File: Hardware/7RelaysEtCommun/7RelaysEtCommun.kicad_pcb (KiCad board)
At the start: 2 copper layers, 67 x 93 mm, 41 parts, among them J1 5VIN, J10 ISP, J2 Conn_01x02_Female, J3 Conn_01x02_Female, J4 Conn_01x02_Female, J5 Conn_01x02_Female, J6 Conn_01x02_Female, J7 Conn_01x02_Female, J8 Conn_01x02_Female, K1 UMS05-1A80-75L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

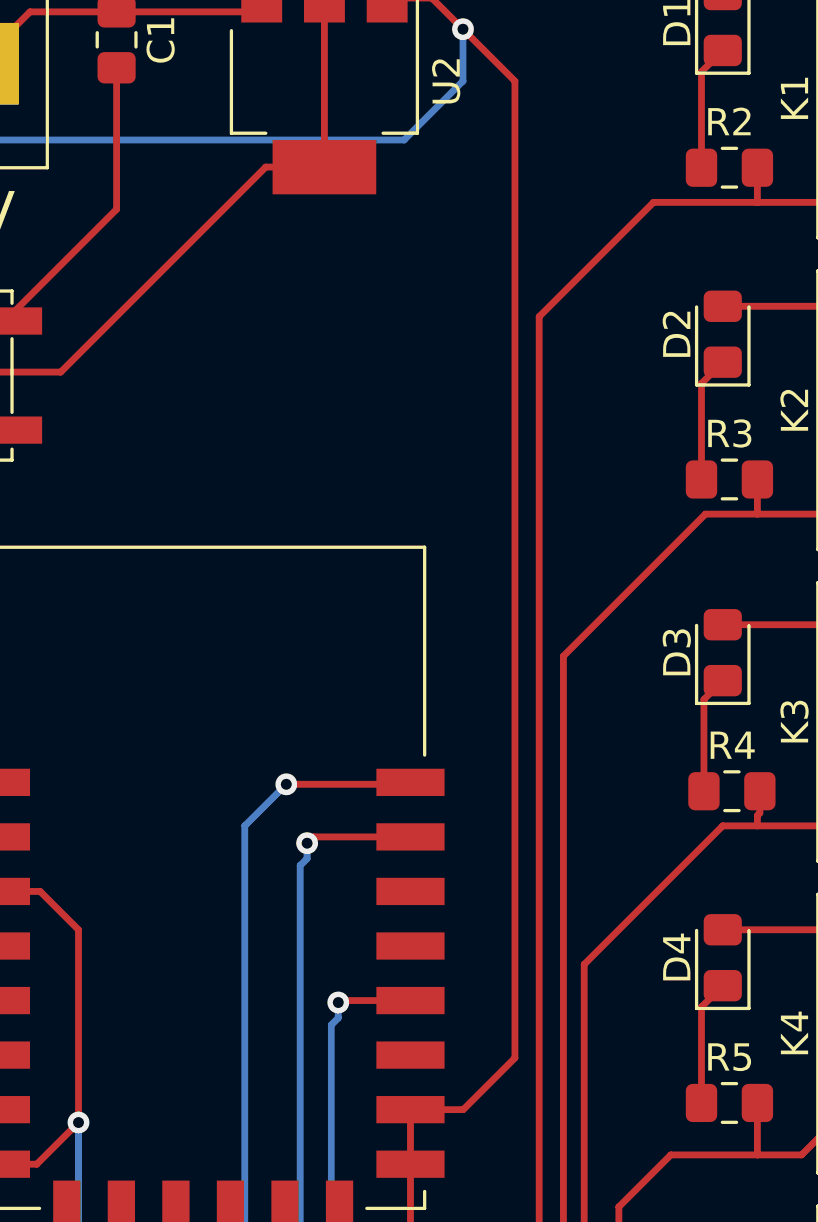
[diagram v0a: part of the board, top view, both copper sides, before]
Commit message: - Modified almost all hardware boards : They were missing a pull-up resistor on GPIO2, which made impossible to flash. - Updated baseBoard.* files
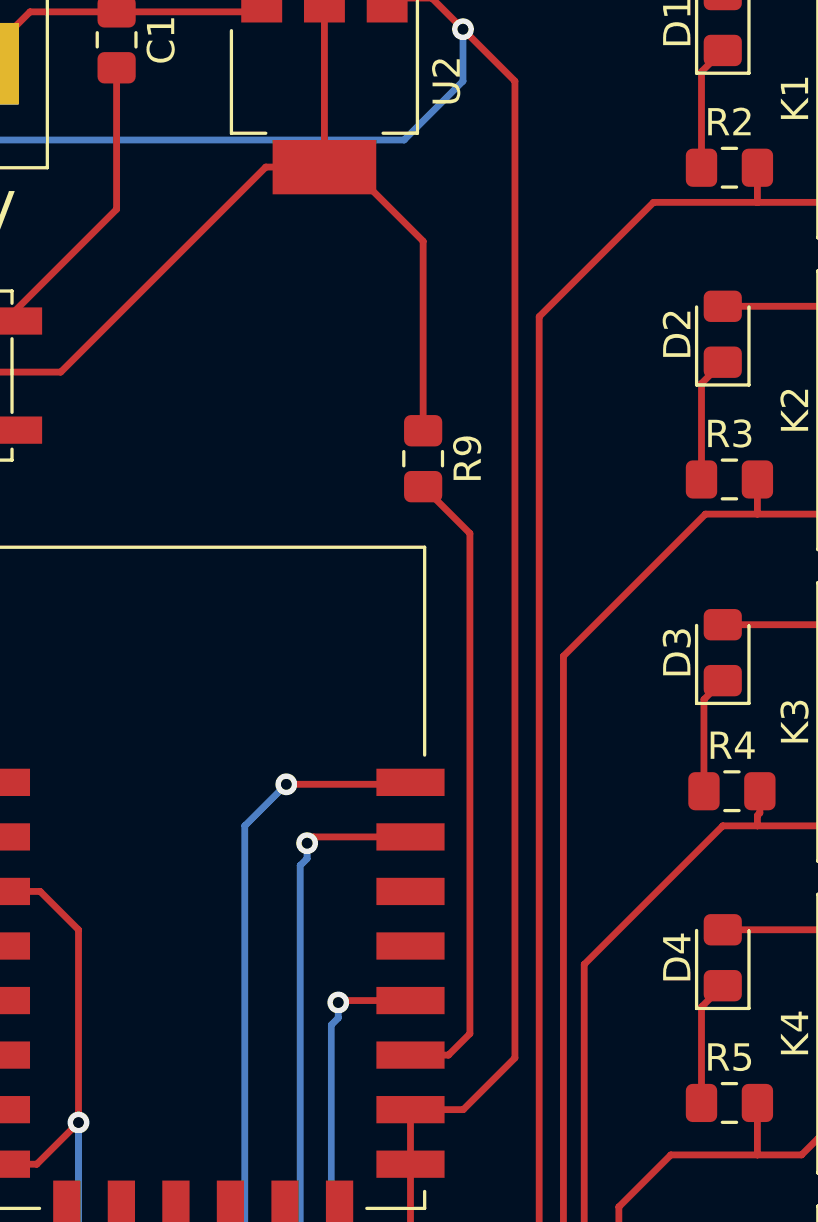
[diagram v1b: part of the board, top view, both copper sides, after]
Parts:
- added R9: 10k, Resistor_SMD:R_0805_2012Metric_Pad1.15x1.40mm_HandSolder, F.Cu at (156.7, 64.0)
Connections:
- U1 pad 15: Net-(U1-Pad15) -> (no net)
- U1 pad 9: Net-(U1-Pad9) -> (no net)
- U3 pad 10: Net-(U3-Pad10) -> (no net)
- U3 pad 11: Net-(U3-Pad11) -> (no net)
- U3 pad 12: Net-(U3-Pad12) -> (no net)
- U3 pad 13: Net-(U3-Pad13) -> (no net)
- U3 pad 14: Net-(U3-Pad14) -> (no net)
- U3 pad 19: Net-(U3-Pad19) -> (no net)
- U3 pad 2: Net-(U3-Pad2) -> (no net)
- U3 pad 20: Net-(U3-Pad20) -> (no net)
- U3 pad 4: Net-(U3-Pad4) -> (no net)
- U3 pad 9: Net-(U3-Pad9) -> (no net)
- U4 pad 11: Net-(U4-Pad11) -> (no net)
- U4 pad 8: Net-(U4-Pad8) -> (no net)
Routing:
- net Net-(R9-Pad2): track 0.00 -> 23.3 mm
- net /3V3: track 136.0 -> 147.7 mm
